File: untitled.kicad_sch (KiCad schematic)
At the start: 15 parts, among them U4 TPS566242DRLR

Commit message: added headers and modified some stuff
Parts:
- removed R23: 100k, Resistor_SMD:R_0201_0603Metric_Pad0.64x0.40mm_HandSolder, symbol Device:R_Small
- removed R24: 20k, Resistor_SMD:R_0201_0603Metric_Pad0.64x0.40mm_HandSolder, symbol Device:R_Small
- added J8: Conn_01x03, symbol Connector_Generic:Conn_01x03
- added Q12: 2N7002, Package_TO_SOT_SMD:SOT-23, symbol Transistor_FET:2N7002
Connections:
- net GND: now also J8.3 (Pin_3)
- net EN: no longer names the net of U4.5 (EN)
- net EN: now also Q12.2 (S)
- new net +5V_EN: J8.1 (Pin_1)
- new net 12V_PG: Q12.1 (G)
- new net 3V3_EN: J8.2 (Pin_2), Q12.3 (D)

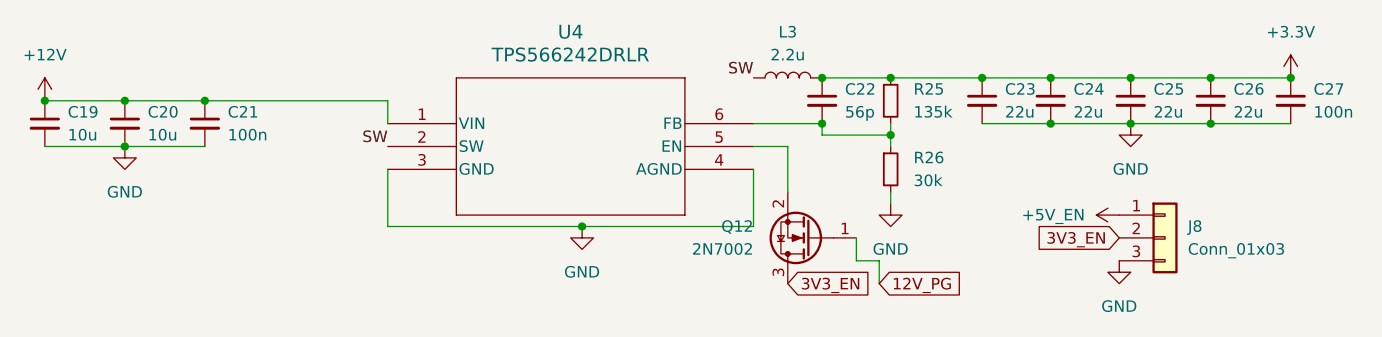
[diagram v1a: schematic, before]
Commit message: added footprints and standardized EN headers
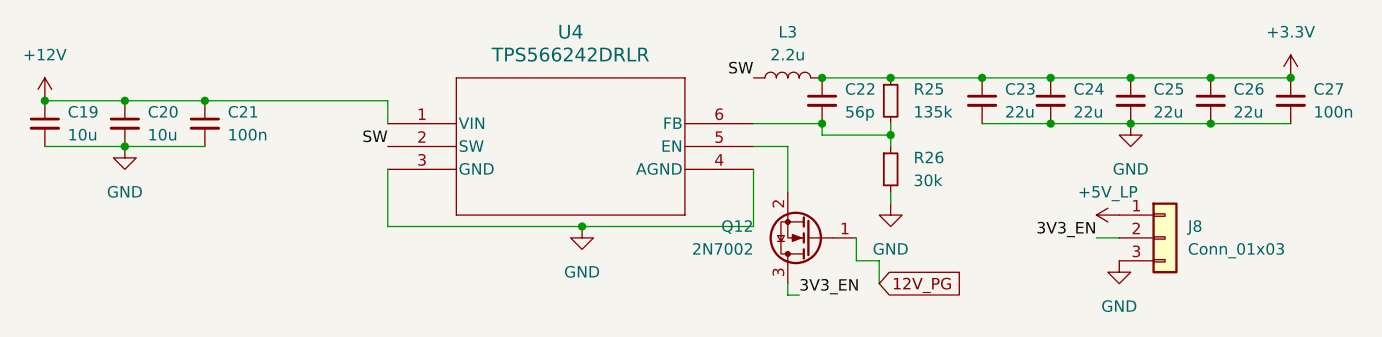
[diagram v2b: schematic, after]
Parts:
- J8: footprint (none) -> Connector_PinHeader_2.54mm:PinHeader_1x03_P2.54mm_Vertical
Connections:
- net +5V_EN renamed +5V_LP
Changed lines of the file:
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@@
+	(wire
+		(pts
+			(xy 100.33 57.15) (xy 100.33 55.88)
+		)
+		(stroke
+			(width 0)
+			(type default)
+		)
+	)
 	(wire
 		(pts
@@
 	(wire
 		(pts
+			(xy 101.6 57.15) (xy 100.33 57.15)
+		)
+		(stroke
+			(width 0)
+			(type default)
+		)
+	)
+	(wire
+		(pts
 			(xy 26.67 40.64) (xy 35.56 40.64)
 		)
@@
 		(pts
 			(xy 96.52 49.53) (xy 96.52 43.18)
+		)
+		(stroke
+			(width 0)
+			(type default)
+		)
+	)
+	(wire
+		(pts
+			(xy 134.62 50.8) (xy 137.16 50.8)
 		)
 		(stroke
@@
 		)
 	)
-	(global_label "3V3_EN"
-		(shape input)
-		(at 100.33 55.88 0)
-		(fields_autoplaced yes)
+	(label "3V3_EN"
+		(at 134.62 50.8 180)
 		(effects
 			(font
 				(size 1.27 1.27)
 			)
-			(justify left)
-		)
-		(property "Intersheetrefs" "${INTERSHEET_REFS}"
-			(at 110.2699 55.88 0)
-			(effects
-				(font
-					(size 1.27 1.27)
-				)
-				(justify left)
-				(hide yes)
-			)
-		)
-	)
-	(global_label "3V3_EN"
-		(shape input)
-		(at 137.16 50.8 180)
-		(fields_autoplaced yes)
+			(justify right bottom)
+		)
+	)
+	(label "3V3_EN"
+		(at 101.6 57.15 0)
 		(effects
 			(font
 				(size 1.27 1.27)
 			)
-			(justify right)
-		)
-		(property "Intersheetrefs" "${INTERSHEET_REFS}"
-			(at 127.2201 50.8 0)
-			(effects
-				(font
-					(size 1.27 1.27)
-				)
-				(justify right)
-				(hide yes)
-			)
+			(justify left bottom)
 		)
 	)
@@
 			)
 		)
-		(property "Value" "+5V_EN"
-			(at 133.35 48.2599 90)
-			(effects
-				(font
-					(size 1.27 1.27)
-				)
-				(justify left)
+		(property "Value" "+5V_LP"
+			(at 135.89 45.72 90)
+			(effects
+				(font
+					(size 1.27 1.27)
+				)
 			)
 		)
@@
 			)
 		)
-		(property "Footprint" ""
+		(property "Footprint" "Connector_PinHeader_2.54mm:PinHeader_1x03_P2.54mm_Vertical"
 			(at 142.24 50.8 0)
 			(effects

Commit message: final push
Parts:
- L3: footprint Capacitor_SMD:C_0201_0603Metric_Pad0.64x0.40mm_HandSolder -> footprints:IND_1217AS-H-2R2N=P3
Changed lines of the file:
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@@
+				)
+			)
+			(project "untitled"
+				(path "/b131ec41-cf91-4589-a70b-8c0de6f53873"
+					(reference "#PWR?")
+					(unit 1)
 				)
 			)
@@
 				)
 			)
+			(project "untitled"
+				(path "/b131ec41-cf91-4589-a70b-8c0de6f53873"
+					(reference "#PWR?")
+					(unit 1)
+				)
+			)
 		)
 	)
@@
 			)
 		)
-		(property "Footprint" "Capacitor_SMD:C_0201_0603Metric_Pad0.64x0.40mm_HandSolder"
+		(property "Footprint" "footprints:IND_1217AS-H-2R2N=P3"
 			(at 100.33 33.02 0)
 			(effects
@@
 				)
 			)
+			(project "untitled"
+				(path "/b131ec41-cf91-4589-a70b-8c0de6f53873"
+					(reference "L?")
+					(unit 1)
+				)
+			)
 		)
 	)
@@
 				)
 			)
+			(project "untitled"
+				(path "/b131ec41-cf91-4589-a70b-8c0de6f53873"
+					(reference "C?")
+					(unit 1)
+				)
+			)
 		)
 	)
@@
 				)
 			)
+			(project "untitled"
+				(path "/b131ec41-cf91-4589-a70b-8c0de6f53873"
+					(reference "C?")
+					(unit 1)
+				)
+			)
 		)
 	)
@@
 				)
 			)
+			(project "untitled"
+				(path "/b131ec41-cf91-4589-a70b-8c0de6f53873"
+					(reference "#PWR?")
+					(unit 1)
+				)
+			)
 		)
 	)
@@
 				)
 			)
+			(project "untitled"
+				(path "/b131ec41-cf91-4589-a70b-8c0de6f53873"
+					(reference "U?")
+					(unit 1)
+				)
+			)
 		)
 	)
@@
 				)
 			)
+			(project "untitled"
+				(path "/b131ec41-cf91-4589-a70b-8c0de6f53873"
+					(reference "J?")
+					(unit 1)
+				)
+			)
 		)
 	)
@@
 				)
 			)
+			(project "untitled"
+				(path "/b131ec41-cf91-4589-a70b-8c0de6f53873"
+					(reference "Q?")
+					(unit 1)
+				)
+			)
 		)
 	)
@@
 				)
 			)
+			(project "untitled"
+				(path "/b131ec41-cf91-4589-a70b-8c0de6f53873"
+					(reference "#PWR?")
+					(unit 1)
+				)
+			)
 		)
 	)
@@
 				)
 			)
+			(project "untitled"
+				(path "/b131ec41-cf91-4589-a70b-8c0de6f53873"
+					(reference "#PWR?")
+					(unit 1)
+				)
+			)
 		)
 	)
@@
 				)
 			)
+			(project "untitled"
+				(path "/b131ec41-cf91-4589-a70b-8c0de6f53873"
+					(reference "C?")
+					(unit 1)
+				)
+			)
 		)
 	)
@@
 				)
 			)
+			(project "untitled"
+				(path "/b131ec41-cf91-4589-a70b-8c0de6f53873"
+					(reference "#PWR?")
+					(unit 1)
+				)
+			)
 		)
 	)
@@
 				)
 			)
+			(project "untitled"
+				(path "/b131ec41-cf91-4589-a70b-8c0de6f53873"
+					(reference "R?")
+					(unit 1)
+				)
+			)
 		)
 	)
@@
 				)
 			)
+			(project "untitled"
+				(path "/b131ec41-cf91-4589-a70b-8c0de6f53873"
+					(reference "C?")
+					(unit 1)
+				)
+			)
 		)
 	)
@@
 				)
 			)
+			(project "untitled"
+				(path "/b131ec41-cf91-4589-a70b-8c0de6f53873"
+					(reference "C?")
+					(unit 1)
+				)
+			)
 		)
 	)
@@
 				)
 			)
+			(project "untitled"
+				(path "/b131ec41-cf91-4589-a70b-8c0de6f53873"
+					(reference "C?")
+					(unit 1)
+				)
+			)
 		)
 	)
@@
 				)
 			)
+			(project "untitled"
+				(path "/b131ec41-cf91-4589-a70b-8c0de6f53873"
+					(reference "C?")
+					(unit 1)
+				)
+			)
 		)
 	)
@@
 				)
 			)
+			(project "untitled"
+				(path "/b131ec41-cf91-4589-a70b-8c0de6f53873"
+					(reference "C?")
+					(unit 1)
+				)
+			)
 		)
 	)
@@
 				)
 			)
+			(project "untitled"
+				(path "/b131ec41-cf91-4589-a70b-8c0de6f53873"
+					(reference "R?")
+					(unit 1)
+				)
+			)
 		)
 	)
@@
 				)
 			)
+			(project "untitled"
+				(path "/b131ec41-cf91-4589-a70b-8c0de6f53873"
+					(reference "C?")
+					(unit 1)
+				)
+			)
 		)
 	)
@@
 				)
 			)
+			(project "untitled"
+				(path "/b131ec41-cf91-4589-a70b-8c0de6f53873"
+					(reference "#PWR?")
+					(unit 1)
+				)
+			)
 		)
 	)
@@
 				)
 			)
-		)
-	)
+			(project "untitled"
+				(path "/b131ec41-cf91-4589-a70b-8c0de6f53873"
+					(reference "#PWR?")
+					(unit 1)
+				)
+			)
+		)
+	)
+	(sheet_instances
+		(path "/"
+			(page "1")
+		)
+	)
+	(embedded_fonts no)
 )

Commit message: fixed footprintns
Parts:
- C19, C20, C21, C22, C23, C24, C25, C26, C27: footprint Capacitor_SMD:C_0201_0603Metric_Pad0.64x0.40mm_HandSolder -> Capacitor_SMD:C_0603_1608Metric_Pad1.08x0.95mm_HandSolder
- R25, R26: footprint Resistor_SMD:R_0201_0603Metric_Pad0.64x0.40mm_HandSolder -> Resistor_SMD:R_0603_1608Metric_Pad0.98x0.95mm_HandSolder
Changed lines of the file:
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@@
 			)
 		)
-		(property "Footprint" "Capacitor_SMD:C_0201_0603Metric_Pad0.64x0.40mm_HandSolder"
+		(property "Footprint" "Capacitor_SMD:C_0603_1608Metric_Pad1.08x0.95mm_HandSolder"
 			(at 147.32 35.56 0)
 			(effects
@@
 			)
 		)
-		(property "Footprint" "Capacitor_SMD:C_0201_0603Metric_Pad0.64x0.40mm_HandSolder"
+		(property "Footprint" "Capacitor_SMD:C_0603_1608Metric_Pad1.08x0.95mm_HandSolder"
 			(at 26.67 38.1 0)
 			(effects
@@
 			)
 		)
-		(property "Footprint" "Capacitor_SMD:C_0201_0603Metric_Pad0.64x0.40mm_HandSolder"
+		(property "Footprint" "Capacitor_SMD:C_0603_1608Metric_Pad1.08x0.95mm_HandSolder"
 			(at 121.92 35.56 0)
 			(effects
@@
 			)
 		)
-		(property "Footprint" "Resistor_SMD:R_0201_0603Metric_Pad0.64x0.40mm_HandSolder"
+		(property "Footprint" "Resistor_SMD:R_0603_1608Metric_Pad0.98x0.95mm_HandSolder"
 			(at 111.76 43.18 0)
 			(effects
@@
 			)
 		)
-		(property "Footprint" "Capacitor_SMD:C_0201_0603Metric_Pad0.64x0.40mm_HandSolder"
+		(property "Footprint" "Capacitor_SMD:C_0603_1608Metric_Pad1.08x0.95mm_HandSolder"
 			(at 104.14 35.56 0)
 			(effects
@@
 			)
 		)
-		(property "Footprint" "Capacitor_SMD:C_0201_0603Metric_Pad0.64x0.40mm_HandSolder"
+		(property "Footprint" "Capacitor_SMD:C_0603_1608Metric_Pad1.08x0.95mm_HandSolder"
 			(at 35.56 38.1 0)
 			(effects
@@
 			)
 		)
-		(property "Footprint" "Capacitor_SMD:C_0201_0603Metric_Pad0.64x0.40mm_HandSolder"
+		(property "Footprint" "Capacitor_SMD:C_0603_1608Metric_Pad1.08x0.95mm_HandSolder"
 			(at 156.21 35.56 0)
 			(effects
@@
 			)
 		)
-		(property "Footprint" "Capacitor_SMD:C_0201_0603Metric_Pad0.64x0.40mm_HandSolder"
+		(property "Footprint" "Capacitor_SMD:C_0603_1608Metric_Pad1.08x0.95mm_HandSolder"
 			(at 17.78 38.1 0)
 			(effects
@@
 			)
 		)
-		(property "Footprint" "Capacitor_SMD:C_0201_0603Metric_Pad0.64x0.40mm_HandSolder"
+		(property "Footprint" "Capacitor_SMD:C_0603_1608Metric_Pad1.08x0.95mm_HandSolder"
 			(at 138.43 35.56 0)
 			(effects
@@
 			)
 		)
-		(property "Footprint" "Resistor_SMD:R_0201_0603Metric_Pad0.64x0.40mm_HandSolder"
+		(property "Footprint" "Resistor_SMD:R_0603_1608Metric_Pad0.98x0.95mm_HandSolder"
 			(at 111.76 35.56 0)
 			(effects
@@
 			)
 		)
-		(property "Footprint" "Capacitor_SMD:C_0201_0603Metric_Pad0.64x0.40mm_HandSolder"
+		(property "Footprint" "Capacitor_SMD:C_0603_1608Metric_Pad1.08x0.95mm_HandSolder"
 			(at 129.54 35.56 0)
 			(effects

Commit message: updated headers
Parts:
- removed J8: Conn_01x03, Connector_PinHeader_2.54mm:PinHeader_1x03_P2.54mm_Vertical, symbol Connector_Generic:Conn_01x03
